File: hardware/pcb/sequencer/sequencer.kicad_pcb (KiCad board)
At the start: 2 copper layers, 77.9 x 161.2 mm, 122 parts, among them J1 Conn_02x08_Odd_Even, J2 Conn_02x08_Odd_Even, SW1 SW_SPST, SW10 SW_SPST, SW11 SW_SPST, SW12 SW_SPST, SW13 SW_SPST, SW14 SW_SPST, SW15 SW_SPST, SW16 SW_SPST, SW17 SW_SPST, SW18 SW_SPST, SW19 SW_SPST, SW2 SW_SPST, SW20 SW_SPST, SW21 SW_SPST, SW22 SW_SPST, SW23 SW_SPST, SW24 SW_SPST, SW25 SW_SPST, SW26 SW_SPST, SW27 SW_SPST, SW28 SW_SPST, SW29 SW_SPST, SW3 SW_SPST, SW30 SW_SPST, SW31 SW_SPST, SW32 SW_SPST, SW4 SW_SPST, SW5 SW_SPST, SW6 SW_SPST, SW7 SW_SPST, SW8 SW_SPST, SW9 SW_SPST

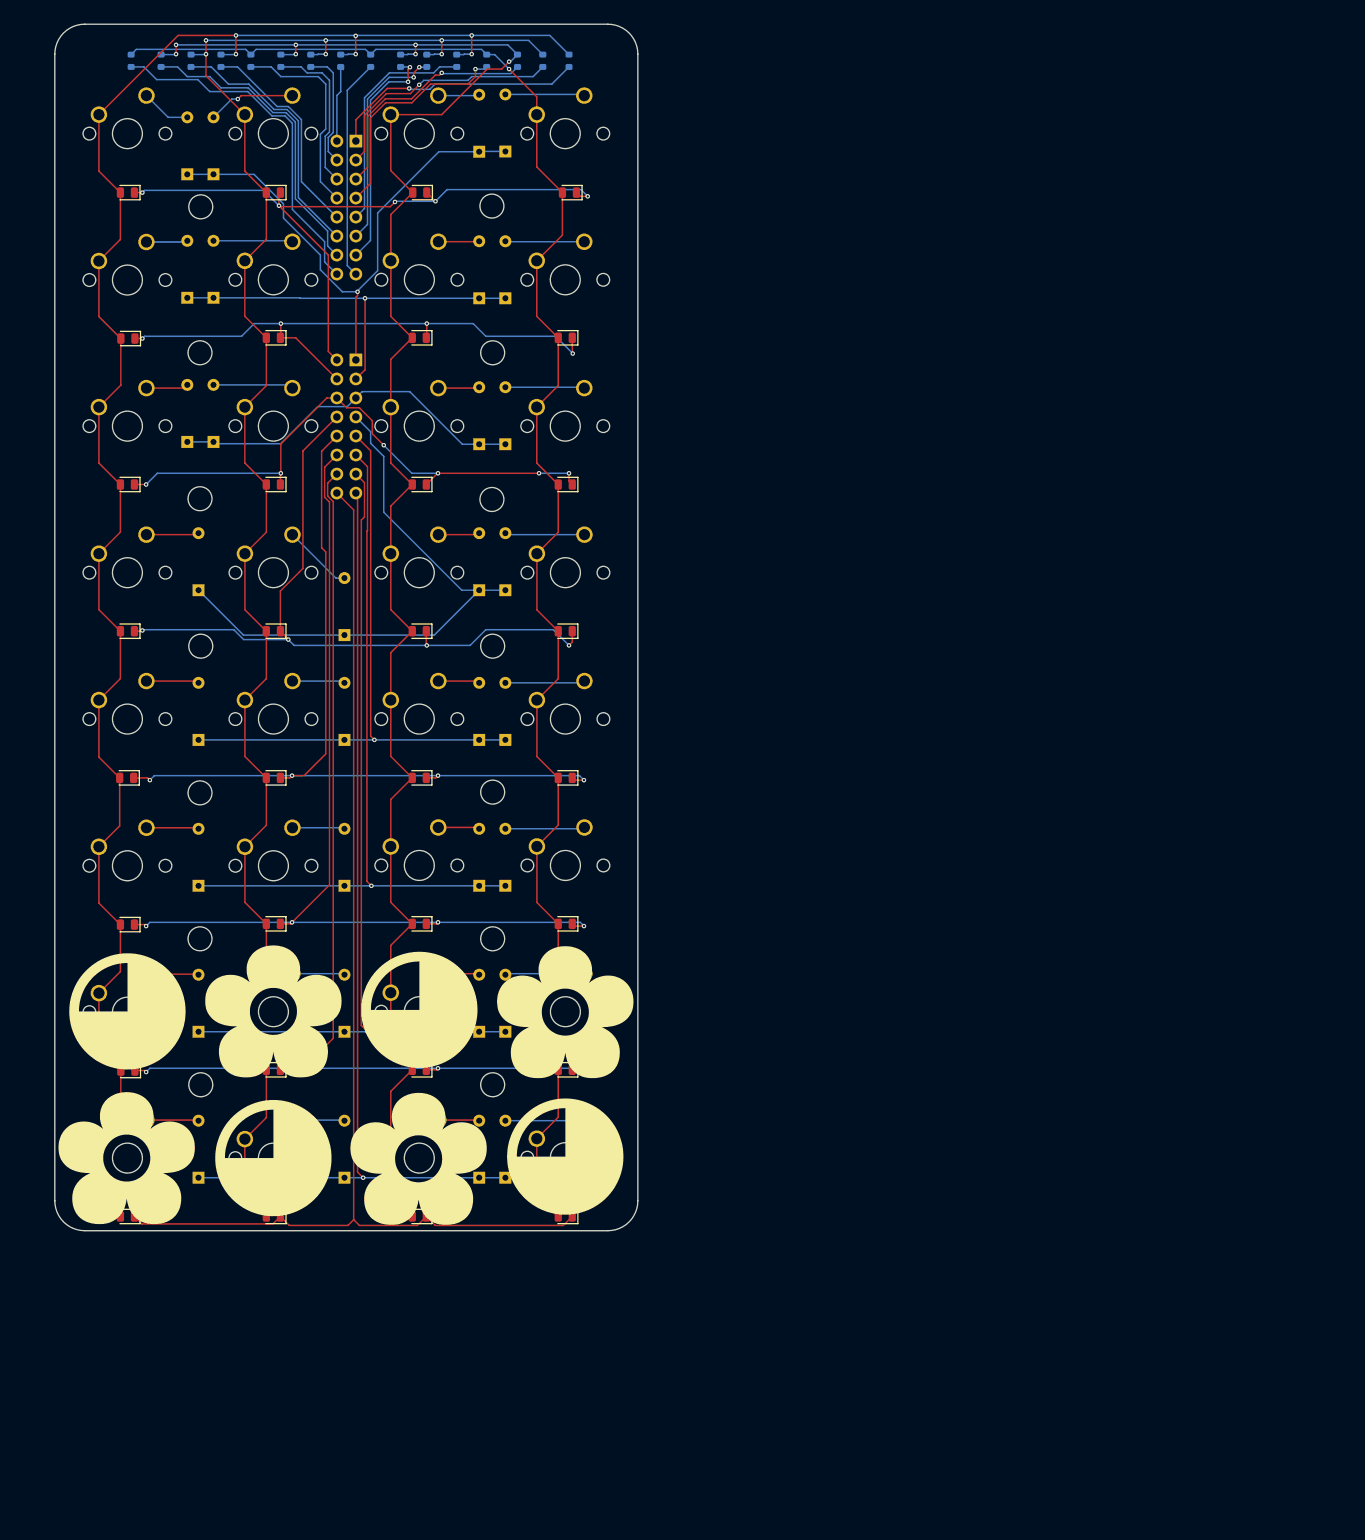
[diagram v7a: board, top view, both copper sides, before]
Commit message: sequencer: update front panel pcb
- switch to through hole leds
- move mounting holes to board edges
- use solder bridges for column selection
- add separate header for led driving

Signed-off-by: Emma Davenport <emma.v.davenport@gmail.com>
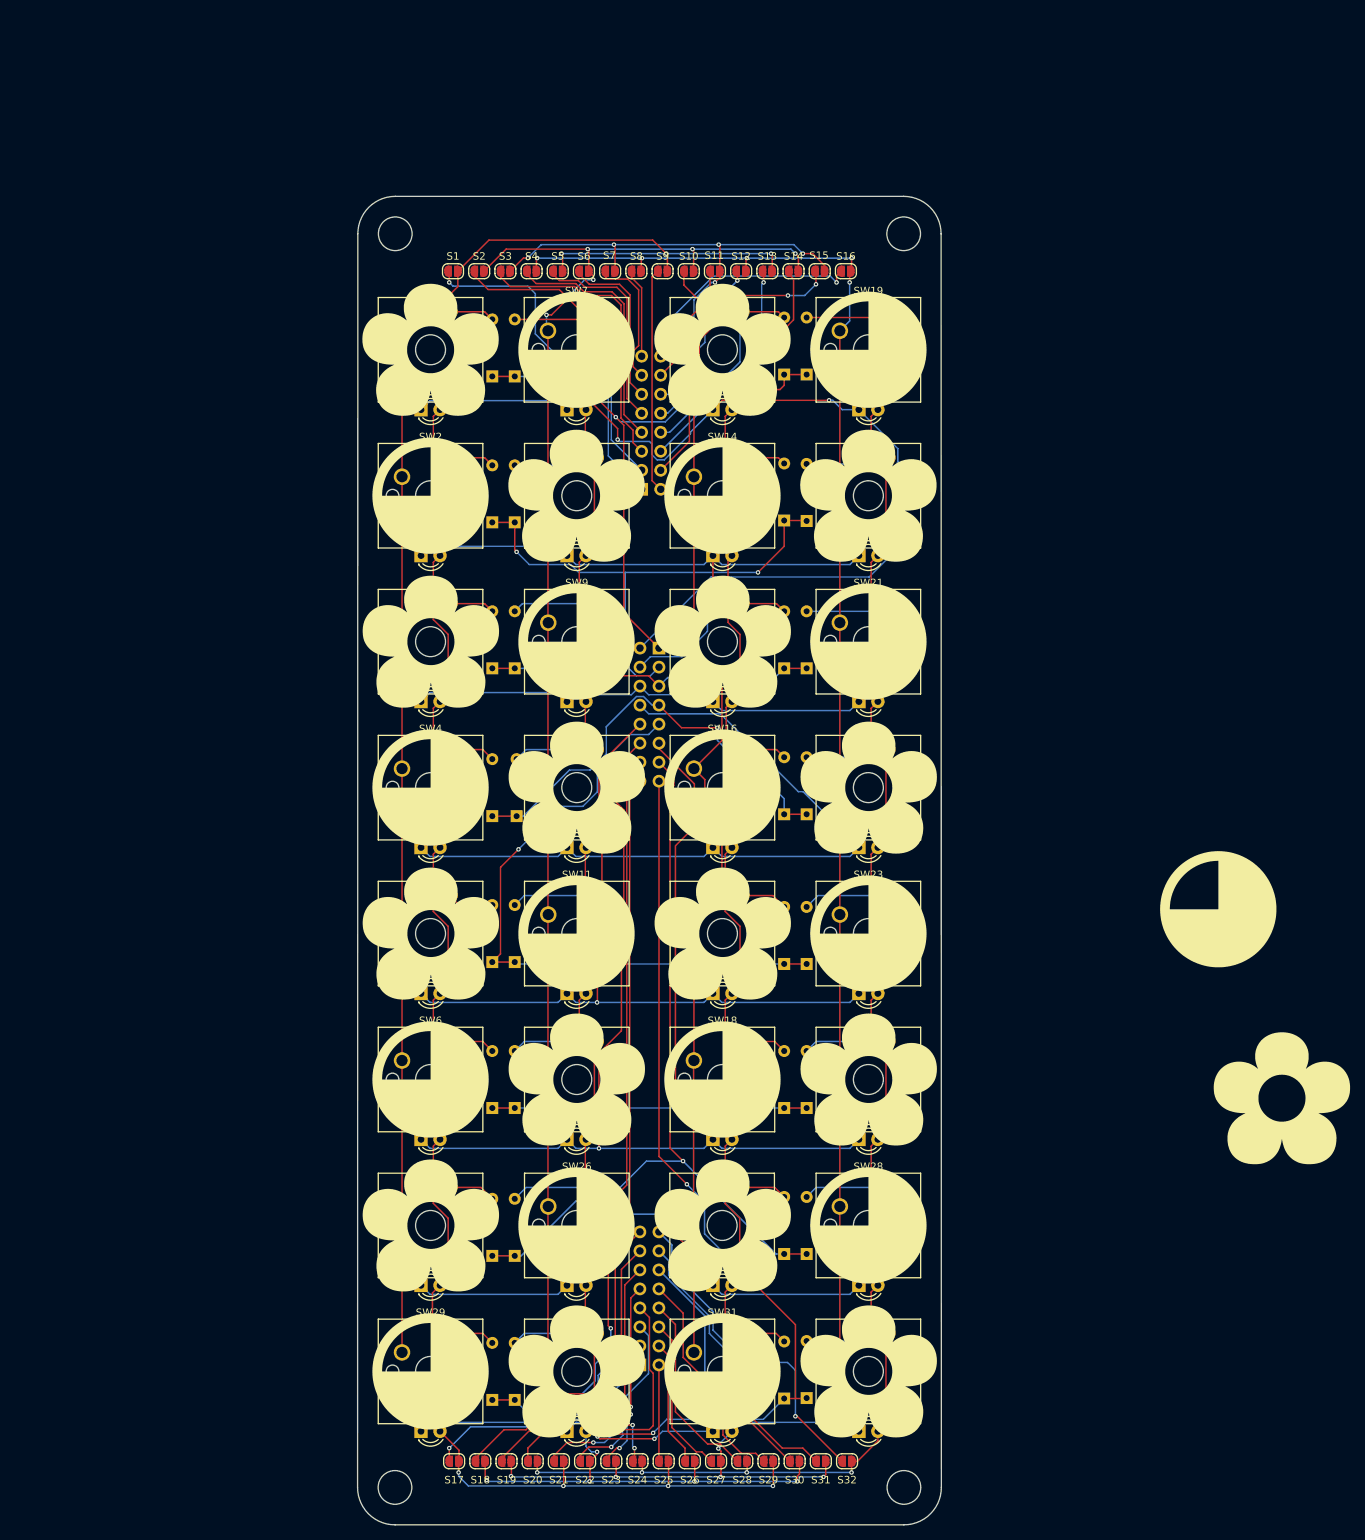
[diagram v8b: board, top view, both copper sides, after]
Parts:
- removed the G*** at (67.5, 151.4)
- removed the G*** at (106.4, 171.1)
- removed the G*** at (67.4, 171.0)
- removed the G*** at (87.0, 151.4)
- removed the G*** at (87.0, 171.0)
- removed the G*** at (126.0, 151.5)
- removed the G*** at (126.0, 170.8)
- removed the G*** at (106.5, 151.2)
- added G***: LOGO, sequencer:circle, F.Cu at (127.5, 102.0)
- added G***: LOGO, sequencer:flower, F.Cu at (127.5, 199.5)
- added G***: LOGO, sequencer:flower, F.Cu at (108.0, 102.0)
- added G***: LOGO, sequencer:circle, F.Cu at (147.0, 82.5)
- added G***: LOGO, sequencer:circle, F.Cu at (166.5, 141.0)
- added G***: LOGO, sequencer:circle, F.Cu at (127.5, 141.0)
- added G***: LOGO, sequencer:circle, F.Cu at (166.5, 102.0)
- added G***: LOGO, sequencer:flower, F.Cu at (127.5, 121.5)
- added G***: LOGO, sequencer:flower, F.Cu at (166.5, 160.5)
- added G***: LOGO, sequencer:flower, F.Cu at (147.0, 102.0)
- added G***: LOGO, sequencer:flower, F.Cu at (221.8, 163.0)
- added G***: LOGO, sequencer:flower, F.Cu at (147.0, 141.0)
- added G***: LOGO, sequencer:circle, F.Cu at (147.0, 160.5)
- added G***: LOGO, sequencer:flower, F.Cu at (127.5, 82.5)
- added G***: LOGO, sequencer:circle, F.Cu at (147.0, 199.5)
- added G***: LOGO, sequencer:circle, F.Cu at (108.0, 160.5)
- added G***: LOGO, sequencer:flower, F.Cu at (108.0, 63.0)
- added G***: LOGO, sequencer:flower, F.Cu at (166.5, 199.5)
- added G***: LOGO, sequencer:flower, F.Cu at (108.0, 141.0)
- added G***: LOGO, sequencer:flower, F.Cu at (166.5, 82.5)
- added G***: LOGO, sequencer:flower, F.Cu at (108.0, 180.0)
- added G***: LOGO, sequencer:circle, F.Cu at (213.2, 137.8)
- added G***: LOGO, sequencer:flower, F.Cu at (147.0, 63.0)
- added G***: LOGO, sequencer:circle, F.Cu at (166.5, 180.0)
- added G***: LOGO, sequencer:circle, F.Cu at (108.0, 121.5)
- added G***: LOGO, sequencer:flower, F.Cu at (127.5, 160.5)
- added G***: LOGO, sequencer:circle, F.Cu at (147.0, 121.5)
- added G***: LOGO, sequencer:circle, F.Cu at (127.5, 180.0)
- added G***: LOGO, sequencer:flower, F.Cu at (166.5, 121.5)
- added G***: LOGO, sequencer:flower, F.Cu at (147.0, 180.0)
- added G***: LOGO, sequencer:circle, F.Cu at (108.0, 199.5)
- added G***: LOGO, sequencer:circle, F.Cu at (166.5, 63.0)
- added G***: LOGO, sequencer:circle, F.Cu at (108.0, 82.5)
- added G***: LOGO, sequencer:circle, F.Cu at (127.5, 63.0)
- added J3: Conn_02x08_Odd_Even, Connector_PinHeader_2.54mm:PinHeader_2x08_P2.54mm_Vertical, B.Cu at (136.0, 198.6)
- added S17: R, Jumper:SolderJumper-2_P1.3mm_Open_RoundedPad1.0x1.5mm, F.Cu at (111.2, 211.5)
- added S18: R, Jumper:SolderJumper-2_P1.3mm_Open_RoundedPad1.0x1.5mm, F.Cu at (114.7, 211.5)
- added S19: R, Jumper:SolderJumper-2_P1.3mm_Open_RoundedPad1.0x1.5mm, F.Cu at (118.2, 211.5)
- added S20: R, Jumper:SolderJumper-2_P1.3mm_Open_RoundedPad1.0x1.5mm, F.Cu at (121.7, 211.5)
- added S21: R, Jumper:SolderJumper-2_P1.3mm_Open_RoundedPad1.0x1.5mm, F.Cu at (125.2, 211.5)
- added S22: R, Jumper:SolderJumper-2_P1.3mm_Open_RoundedPad1.0x1.5mm, F.Cu at (128.7, 211.5)
- added S23: R, Jumper:SolderJumper-2_P1.3mm_Open_RoundedPad1.0x1.5mm, F.Cu at (132.2, 211.5)
- added S24: R, Jumper:SolderJumper-2_P1.3mm_Open_RoundedPad1.0x1.5mm, F.Cu at (135.7, 211.5)
- added S25: R, Jumper:SolderJumper-2_P1.3mm_Open_RoundedPad1.0x1.5mm, F.Cu at (139.2, 211.5)
- added S26: R, Jumper:SolderJumper-2_P1.3mm_Open_RoundedPad1.0x1.5mm, F.Cu at (142.7, 211.5)
- added S27: R, Jumper:SolderJumper-2_P1.3mm_Open_RoundedPad1.0x1.5mm, F.Cu at (146.2, 211.5)
- added S28: R, Jumper:SolderJumper-2_P1.3mm_Open_RoundedPad1.0x1.5mm, F.Cu at (149.7, 211.5)
- added S29: R, Jumper:SolderJumper-2_P1.3mm_Open_RoundedPad1.0x1.5mm, F.Cu at (153.2, 211.5)
- added S30: R, Jumper:SolderJumper-2_P1.3mm_Open_RoundedPad1.0x1.5mm, F.Cu at (156.7, 211.5)
- added S31: R, Jumper:SolderJumper-2_P1.3mm_Open_RoundedPad1.0x1.5mm, F.Cu at (160.2, 211.5)
- added S32: R, Jumper:SolderJumper-2_P1.3mm_Open_RoundedPad1.0x1.5mm, F.Cu at (163.7, 211.5)
- D25, D26, D27, D28, D29, D30, D31, D32, D33, D34, D35, D36, D37, D38, D39, D40, D41, D42, D43, D44, D45, D46, D47, D48, D57, D58, D59, D60, D61, D62, D63, D64: footprint LED_SMD:LED_0805_2012Metric -> LED_THT:LED_D3.0mm
- S1, S10, S11, S12, S13, S14, S15, S16, S2, S3, S4, S5, S6, S7, S8, S9: footprint Resistor_SMD:R_0603_1608Metric -> Jumper:SolderJumper-2_P1.3mm_Open_RoundedPad1.0x1.5mm; moved to F.Cu
- moved S16 99.6 mm to (163.5, 52.5), turned to 0 degrees
- moved S15 92.4 mm to (160.0, 52.5), turned to 0 degrees
- moved S14 85.3 mm to (156.5, 52.5), turned to 0 degrees
- moved S13 78.2 mm to (153.0, 52.5), turned to 0 degrees
- moved S12 71.3 mm to (149.5, 52.5), turned to 0 degrees
- moved S11 64.5 mm to (146.0, 52.5), turned to 0 degrees
- moved J1 60.2 mm to (136.2, 81.6), turned to 0 degrees
- moved S10 57.8 mm to (142.5, 52.5), turned to 0 degrees
- moved J2 55.9 mm to (138.5, 102.9)
- moved S9 51.4 mm to (139.0, 52.5), turned to 0 degrees
- moved D3 50.8 mm to (116.2, 105.6)
- moved D2 50.6 mm to (116.2, 86.1)
- moved D15 50.6 mm to (155.2, 105.6)
- moved D16 50.6 mm to (155.2, 125.1)
- moved D17 50.6 mm to (155.2, 145.1)
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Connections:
- D25 pad 2: C1 -> C5
- D26 pad 2: C1 -> C5
- D27 pad 2: C1 -> C5
- D28 pad 2: C1 -> C5
- D29 pad 2: C1 -> C5
- D30 pad 2: C1 -> C5
- D31 pad 2: C2 -> C6
- D32 pad 2: C2 -> C6
- D33 pad 2: C2 -> C6
- D34 pad 2: C2 -> C6
- D35 pad 2: C2 -> C6
- D36 pad 2: C2 -> C6
- D37 pad 2: C3 -> C7
- D38 pad 2: C3 -> C7
- D39 pad 2: C3 -> C7
- D40 pad 2: C3 -> C7
- D41 pad 2: C3 -> C7
- D42 pad 2: C3 -> C7
- D43 pad 2: C4 -> C8
- D44 pad 2: C4 -> C8
- D45 pad 2: C4 -> C8
- D46 pad 2: C4 -> C8
- D47 pad 2: C4 -> C8
- D48 pad 2: C4 -> C8
- D57 pad 2: C1 -> C5
- D58 pad 2: C2 -> C6
- D59 pad 2: C3 -> C7
- D60 pad 2: C4 -> C8
- D61 pad 2: C1 -> C5
- D62 pad 2: C2 -> C6
- D63 pad 2: C3 -> C7
- D64 pad 2: C4 -> C8
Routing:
- net C5: track 0.00 -> 207.7 mm, vias 0 -> 4
- net C6: track 0.00 -> 203.3 mm, vias 0 -> 5
- net C7: track 0.00 -> 202.7 mm, vias 0 -> 5
- net C8: track 0.00 -> 201.9 mm, vias 0 -> 4
- net L16: track 0.00 -> 44.7 mm, vias 0 -> 1
- net L15: track 0.00 -> 38.4 mm, vias 0 -> 1
- net L4: track 0.00 -> 37.9 mm, vias 0 -> 2
- net O9: track 91.9 -> 129.6 mm, vias 5 -> 2
- net C3: track 241.3 -> 205.0 mm, vias 7 -> 5
- net L8: track 0.00 -> 35.1 mm, vias 0 -> 2
- net L14: track 0.00 -> 34.2 mm, vias 0 -> 1
- net L7: track 0.00 -> 33.0 mm, vias 0 -> 2
- net C1: track 246.9 -> 214.0 mm, vias 6 -> 3
- net C2: track 232.6 -> 200.1 mm
- net C4: track 226.1 -> 194.2 mm, vias 1 -> 5
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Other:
- board size 77.9 x 161.2 mm -> 78 x 177.5 mm
- board text removed: "ADDRESS"
- board text removed: "DATA"
- board text removed: "S15"
- board text removed: "SOLDER BRIDGES 1: S1 S5 S9 S13 2: S2 S6 S10 S14 3: S3 S7 S11 S15 4: S4 S8 S12 S16"
